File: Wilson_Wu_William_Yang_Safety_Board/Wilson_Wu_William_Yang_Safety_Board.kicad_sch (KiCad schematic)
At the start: 17 parts, among them J1 22035035, J2 XT60-M, J3 XT60-M, J4 M22-7130442, J5 Molex Micro-Fit 4 Pin, J6 430450200, J7 430450200, K1 Fujitsu_FTR-LYAA005x, Q1 IRLML6344TRPBF, U2 MCP2562-E/P, U3 MCP6286T-E/OT, U4 4002, U5 100 ohm

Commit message: edited board
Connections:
- net Boost converter renamed boost converter
- net power_in n: no longer names the net of J2.N (NEG), K1.13
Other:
- moved on the sheet: J2
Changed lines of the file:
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@@
 	(wire
 		(pts
-			(xy 21.59 29.21) (xy 21.59 26.67)
+			(xy 265.43 67.31) (xy 267.97 67.31)
 		)
 		(stroke
@@
 	(wire
 		(pts
-			(xy -33.02 29.21) (xy 21.59 29.21)
-		)
-		(stroke
-			(width 0)
-			(type default)
-		)
-	)
-	(wire
-		(pts
 			(xy 182.88 81.28) (xy 196.85 81.28)
 		)
@@
 	(wire
 		(pts
-			(xy 24.13 26.67) (xy 24.13 31.75)
-		)
-		(stroke
-			(width 0)
-			(type default)
-		)
-	)
-	(wire
-		(pts
 			(xy 69.85 22.86) (xy 71.12 22.86)
 		)
@@
 	(wire
 		(pts
+			(xy 265.43 60.96) (xy 303.53 60.96)
+		)
+		(stroke
+			(width 0)
+			(type default)
+		)
+	)
+	(wire
+		(pts
 			(xy 69.85 25.4) (xy 86.36 25.4)
 		)
@@
 	(wire
 		(pts
-			(xy 234.95 69.85) (xy 237.49 69.85)
+			(xy 234.95 69.85) (xy 267.97 69.85)
 		)
 		(stroke
@@
 		(pts
 			(xy 180.34 35.56) (xy 180.34 39.37)
+		)
+		(stroke
+			(width 0)
+			(type default)
+		)
+	)
+	(wire
+		(pts
+			(xy 265.43 67.31) (xy 265.43 60.96)
 		)
 		(stroke
@@
 		)
 	)
-	(global_label "Boost converter"
-		(shape input)
-		(at -33.02 29.21 180)
-		(fields_autoplaced yes)
-		(effects
-			(font
-				(size 1.27 1.27)
-			)
-			(justify right)
-		)
-		(property "Intersheetrefs" "${INTERSHEET_REFS}"
-			(at -51.1241 29.21 0)
-			(effects
-				(font
-					(size 1.27 1.27)
-				)
-				(justify right)
-				(hide yes)
-			)
-		)
-	)
 	(global_label "CAN_H"
 		(shape input)
@@
 		)
 	)
-	(global_label "power_in n"
+	(global_label "boost converter"
 		(shape input)
-		(at 237.49 69.85 0)
+		(at 303.53 60.96 0)
 		(fields_autoplaced yes)
 		(effects
@@
 		)
 		(property "Intersheetrefs" "${INTERSHEET_REFS}"
-			(at 250.8165 69.85 0)
+			(at 321.5131 60.96 0)
 			(effects
 				(font
@@
 				)
 				(justify left)
-				(hide yes)
-			)
-		)
-	)
-	(global_label "power_in n"
-		(shape input)
-		(at 24.13 31.75 270)
-		(fields_autoplaced yes)
-		(effects
-			(font
-				(size 1.27 1.27)
-			)
-			(justify right)
-		)
-		(property "Intersheetrefs" "${INTERSHEET_REFS}"
-			(at 24.13 45.0765 90)
-			(effects
-				(font
-					(size 1.27 1.27)
-				)
-				(justify right)
 				(hide yes)
 			)
@@
 	(symbol
 		(lib_id "SMV_Custom:XT60-M")
-		(at 24.13 21.59 90)
+		(at 273.05 69.85 0)
 		(unit 1)
 		(exclude_from_sim no)
@@
 		(fields_autoplaced yes)
 		(property "Reference" "J2"
-			(at 27.94 16.5099 90)
+			(at 278.1301 73.66 90)
 			(effects
 				(font
@@
 		)
 		(property "Value" "XT60-M"
-			(at 27.94 19.0499 90)
+			(at 275.5901 73.66 90)
 			(effects
 				(font
@@
 		)
 		(property "Footprint" "SMV_Connectors:AMASS_XT60-M"
-			(at 24.13 21.59 0)
+			(at 273.05 69.85 0)
 			(effects
 				(font
@@
 		)
 		(property "Datasheet" ""
-			(at 24.13 21.59 0)
+			(at 273.05 69.85 0)
 			(effects
 				(font
@@
 		)
 		(property "Description" ""
-			(at 24.13 21.59 0)
+			(at 273.05 69.85 0)
 			(effects
 				(font
@@
 		)
 		(property "MF" "AMASS"
-			(at 24.13 21.59 0)
+			(at 273.05 69.85 0)
 			(effects
 				(font
@@
 		)
 		(property "MAXIMUM_PACKAGE_HEIGHT" "16.00 mm"
-			(at 24.13 21.59 0)
+			(at 273.05 69.85 0)
 			(effects
 				(font
@@
 		)
 		(property "Package" "Package"
-			(at 24.13 21.59 0)
+			(at 273.05 69.85 0)
 			(effects
 				(font
@@
 		)
 		(property "Price" "None"
-			(at 24.13 21.59 0)
+			(at 273.05 69.85 0)
 			(effects
 				(font
@@
 		)
 		(property "Check_prices" "https://www.snapeda.com/parts/XT60-M/AMASS/view-part/?ref=eda"
-			(at 24.13 21.59 0)
+			(at 273.05 69.85 0)
 			(effects
 				(font
@@
 		)
 		(property "STANDARD" "IPC 7351B"
-			(at 24.13 21.59 0)
+			(at 273.05 69.85 0)
 			(effects
 				(font
@@
 		)
 		(property "PARTREV" "V1.2"
-			(at 24.13 21.59 0)
+			(at 273.05 69.85 0)
 			(effects
 				(font
@@
 		)
 		(property "SnapEDA_Link" "https://www.snapeda.com/parts/XT60-M/AMASS/view-part/?ref=snap"
-			(at 24.13 21.59 0)
+			(at 273.05 69.85 0)
 			(effects
 				(font
@@
 		)
 		(property "MP" "XT60-M"
-			(at 24.13 21.59 0)
+			(at 273.05 69.85 0)
 			(effects
 				(font
@@
 		)
 		(property "Description_1" "\n                        \n                            Plug; DC supply; XT60; male; PIN: 2; for cable; soldered; 30A; 500V\n                        \n"
-			(at 24.13 21.59 0)
+			(at 273.05 69.85 0)
 			(effects
 				(font
@@
 		)
 		(property "Availability" "Not in stock"
-			(at 24.13 21.59 0)
+			(at 273.05 69.85 0)
 			(effects
 				(font
@@
 		)
 		(property "MANUFACTURER" "AMASS"
-			(at 24.13 21.59 0)
-			(effects
-				(font
+			(at 273.05 69.85 0)
+			(effects
+				(font

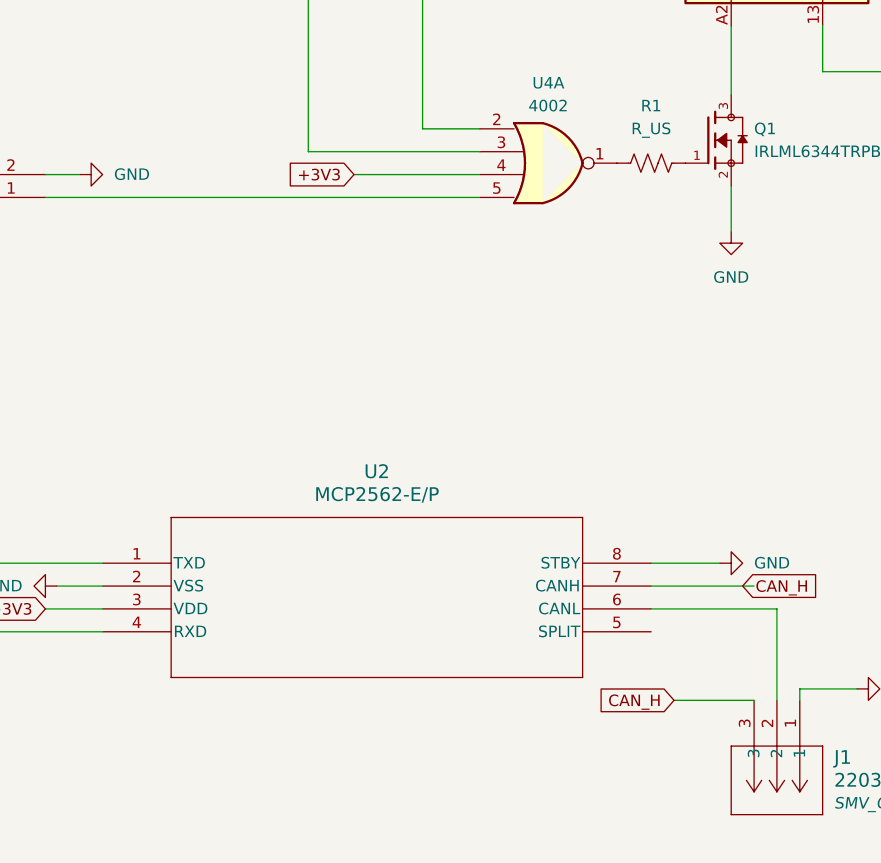
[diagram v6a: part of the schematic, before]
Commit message: edited sch
based on soloman's advice
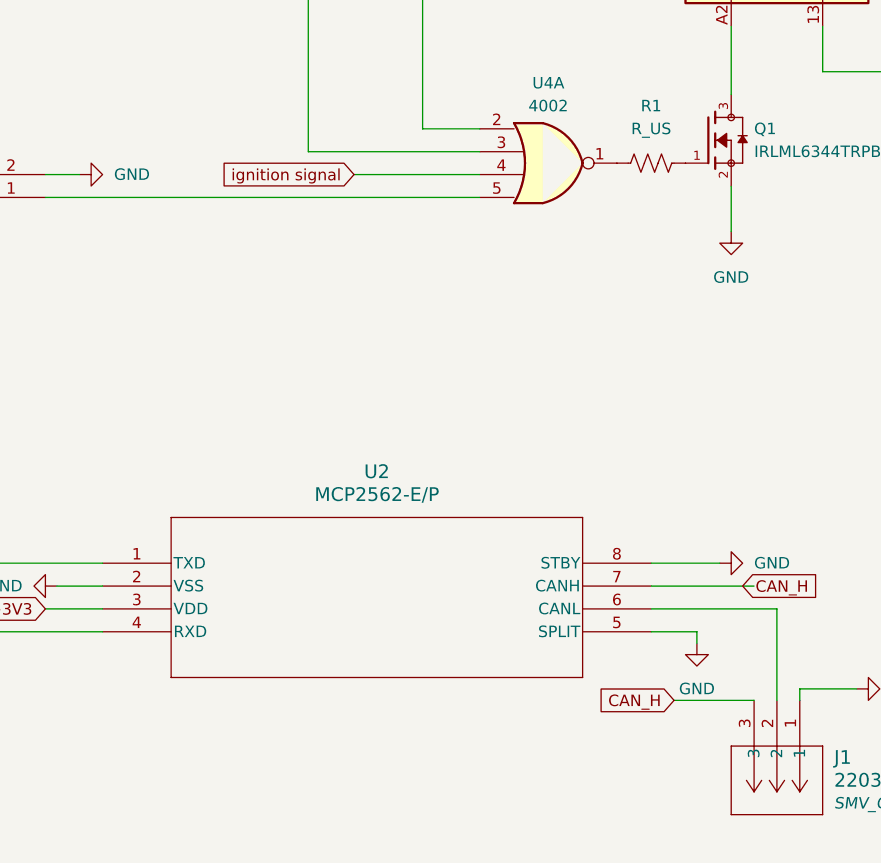
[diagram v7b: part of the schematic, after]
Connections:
- net +3V3: no longer U4.4
- net GND: now also U2.5 (SPLIT)
- new net ignition signal: U4.4
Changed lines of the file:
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@@
+	(wire
+		(pts
+			(xy 215.9 132.08) (xy 220.98 132.08)
+		)
+		(stroke
+			(width 0)
+			(type default)
+		)
+	)
 	(wire
 		(pts
@@
 	(wire
 		(pts
-			(xy 229.87 129.54) (xy 215.9 129.54)
+			(xy 220.98 132.08) (xy 220.98 133.35)
 		)
 		(stroke
@@
 	(wire
 		(pts
-			(xy 83.82 111.76) (xy 83.82 123.19)
+			(xy 229.87 129.54) (xy 215.9 129.54)
 		)
 		(stroke
@@
 	(wire
 		(pts
-			(xy 134.62 111.76) (xy 83.82 111.76)
+			(xy 83.82 111.76) (xy 83.82 123.19)
 		)
 		(stroke
@@
 	(wire
 		(pts
-			(xy 36.83 153.67) (xy 38.1 153.67)
+			(xy 134.62 111.76) (xy 83.82 111.76)
 		)
 		(stroke
@@
 	(wire
 		(pts
-			(xy 92.71 57.15) (xy 92.71 25.4)
+			(xy 36.83 153.67) (xy 38.1 153.67)
 		)
 		(stroke
@@
 	(wire
 		(pts
-			(xy 83.82 128.27) (xy 83.82 139.7)
+			(xy 92.71 57.15) (xy 92.71 25.4)
 		)
 		(stroke
@@
 	(wire
 		(pts
-			(xy 229.87 129.54) (xy 229.87 139.7)
+			(xy 83.82 128.27) (xy 83.82 139.7)
 		)
 		(stroke
@@
 		)
 	)
+	(wire
+		(pts
+			(xy 229.87 129.54) (xy 229.87 139.7)
+		)
+		(stroke
+			(width 0)
+			(type default)
+		)
+	)
 	(global_label "+3V3"
 		(shape input)
@@
 		)
 	)
-	(global_label "+3V3"
+	(global_label "ignition signal"
 		(shape input)
 		(at 182.88 81.28 180)
@@
 		)
 		(property "Intersheetrefs" "${INTERSHEET_REFS}"
-			(at 174.8148 81.28 0)
+			(at 166.046 81.28 0)
 			(effects
 				(font
@@
 					(unit 1)
 				)
+			)
+		)
+	)
+	(symbol
+		(lib_id "power:GND")
+		(at 220.98 133.35 0)
+		(unit 1)
+		(exclude_from_sim no)
+		(in_bom yes)
+		(on_board yes)
+		(dnp no)
+		(fields_autoplaced yes)
+		(property "Reference" "#PWR013"
+			(at 220.98 139.7 0)
+			(effects
+				(font
+					(size 1.27 1.27)
+				)
+				(hide yes)
+			)
+		)
+		(property "Value" "GND"
+			(at 220.98 138.43 0)
+			(effects
+				(font
+					(size 1.27 1.27)
+				)
+			)
+		)
+		(property "Footprint" ""
+			(at 220.98 133.35 0)
+			(effects
+				(font
+					(size 1.27 1.27)
+				)
+				(hide yes)
+			)
+		)
+		(property "Datasheet" ""
+			(at 220.98 133.35 0)
+			(effects
+				(font
+					(size 1.27 1.27)
+				)
+				(hide yes)
+			)
+		)
+		(property "Description" "Power symbol creates a global label with name \"GND\" , ground"
+			(at 220.98 133.35 0)
+			(effects
+				(font
+					(size 1.27 1.27)
+				)
+				(hide yes)
+			)
+		)
+		(pin "1"
+		)
+		(instances
+			(project ""
+				(path "/fa857c32-0741-4b91-b122-1a57686bb514"
+					(reference "#PWR013")
+					(unit 1)
+				)

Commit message: update
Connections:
- net +3.3V: no longer J5.2, R_1.1
- new net +3V0: J5.2, R_1.1
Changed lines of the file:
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@@
+	)
+	(junction
+		(at 49.53 57.15)
+		(diameter 0)
+		(color 0 0 0 0)
 	)
 	(junction
@@
 		(pts
 			(xy 234.95 69.85) (xy 267.97 69.85)
+		)
+		(stroke
+			(width 0)
+			(type default)
+		)
+	)
+	(wire
+		(pts
+			(xy 38.1 57.15) (xy 49.53 57.15)
 		)
 		(stroke
@@
 	)
 	(symbol
+		(lib_id "power:+3V0")
+		(at 38.1 57.15 90)
+		(unit 1)
+		(exclude_from_sim no)
+		(in_bom yes)
+		(on_board yes)
+		(dnp no)
+		(fields_autoplaced yes)
+		(property "Reference" "#PWR09"
+			(at 41.91 57.15 0)
+			(effects
+				(font
+					(size 1.27 1.27)
+				)
+				(hide yes)
+			)
+		)
+		(property "Value" "+3V0"
+			(at 34.29 57.1499 90)
+			(effects
+				(font
+					(size 1.27 1.27)
+				)
+				(justify left)
+			)
+		)
+		(property "Footprint" ""
+			(at 38.1 57.15 0)
+			(effects
+				(font
+					(size 1.27 1.27)
+				)
+				(hide yes)
+			)
+		)
+		(property "Datasheet" ""
+			(at 38.1 57.15 0)
+			(effects
+				(font
+					(size 1.27 1.27)
+				)
+				(hide yes)
+			)
+		)
+		(property "Description" "Power symbol creates a global label with name \"+3V0\""
+			(at 38.1 57.15 0)
+			(effects
+				(font
+					(size 1.27 1.27)
+				)
+				(hide yes)
+			)
+		)
+		(pin "1"
+		)
+		(instances
+			(project ""
+				(path "/fa857c32-0741-4b91-b122-1a57686bb514"
+					(reference "#PWR09")
+					(unit 1)
+				)
+			)
+		)
+	)
+	(symbol
 		(lib_id "power:GND")
 		(at 149.86 127 270)
@@
 	)
 	(symbol
-		(lib_id "power:+3.3V")
-		(at 48.26 25.4 90)
-		(unit 1)
-		(exclude_from_sim no)
-		(in_bom yes)
-		(on_board yes)
-		(dnp no)
-		(fields_autoplaced yes)
-		(property "Reference" "#PWR09"
-			(at 52.07 25.4 0)
-			(effects
-				(font
-					(size 1.27 1.27)
-				)
-				(hide yes)
-			)
-		)
-		(property "Value" "+3.3V"
-			(at 44.45 25.3999 90)
-			(effects
-				(font
-					(size 1.27 1.27)
-				)
-				(justify left)
-			)
-		)
-		(property "Footprint" ""
-			(at 48.26 25.4 0)
-			(effects
-				(font
-					(size 1.27 1.27)
-				)
-				(hide yes)
-			)
-		)
-		(property "Datasheet" ""
-			(at 48.26 25.4 0)
-			(effects
-				(font
-					(size 1.27 1.27)
-				)
-				(hide yes)
-			)
-		)
-		(property "Description" "Power symbol creates a global label with name \"+3.3V\""
-			(at 48.26 25.4 0)
-			(effects
-				(font
-					(size 1.27 1.27)
-				)
-				(hide yes)
-			)
-		)
-		(pin "1"
-		)
-		(instances
-			(project ""
-				(path "/fa857c32-0741-4b91-b122-1a57686bb514"
-					(reference "#PWR09")
-					(unit 1)
-				)
-			)
-		)
-	)
-	(symbol
 		(lib_id "4xxx:4002")
 		(at 204.47 80.01 0)
@@
 			)
 		)
-		(property "Description" "100 ohm potentiometer for hydrogen sensor bridge circuit"
+		(property "Description" "100 ohm potentiometer for hydrogen sensor bridge circuit: https://www.digikey.com/en/products/detail/vishay-sfernice/RSSD50373C1000JB01/10735157"
 			(at 76.2 54.61 0)
 			(effects
